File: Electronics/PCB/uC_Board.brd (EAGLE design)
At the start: 100 x 80 mm, 12 parts

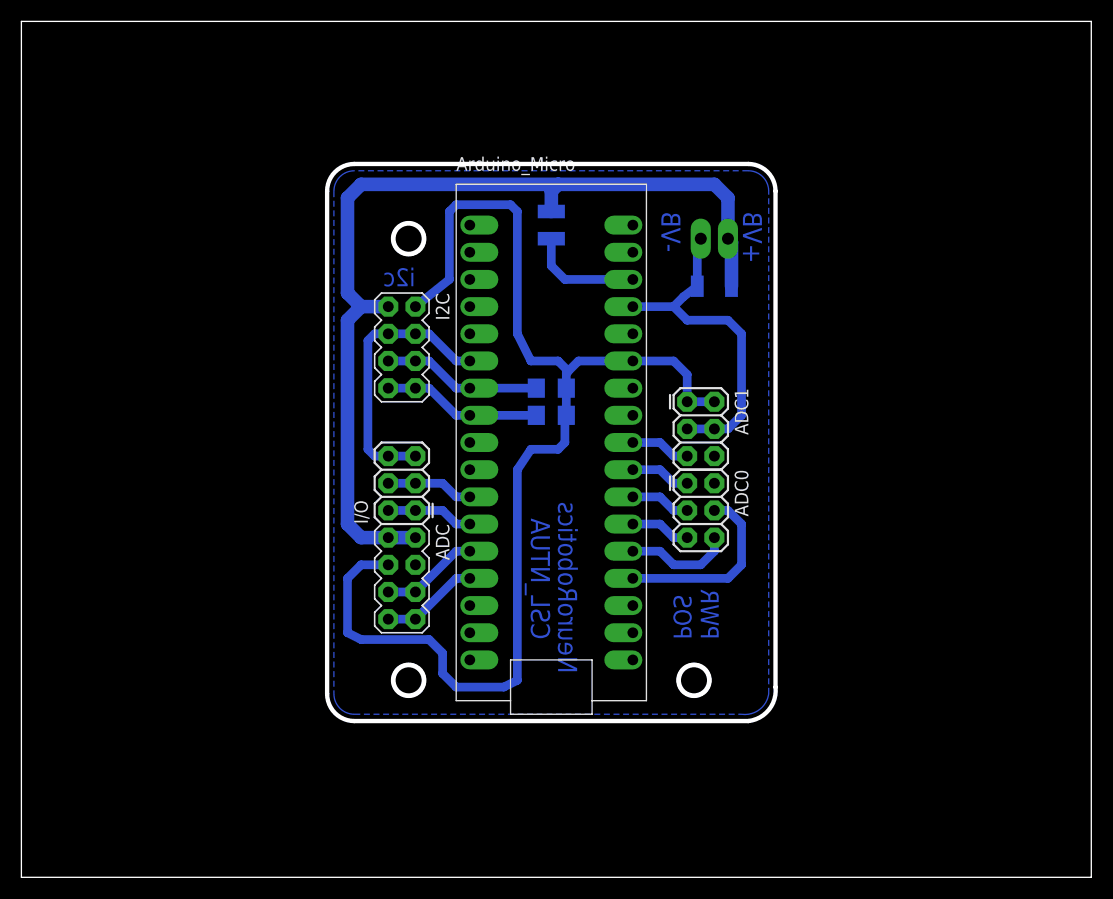
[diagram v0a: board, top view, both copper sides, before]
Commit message: Add new PCB for RC and AX12 servo.
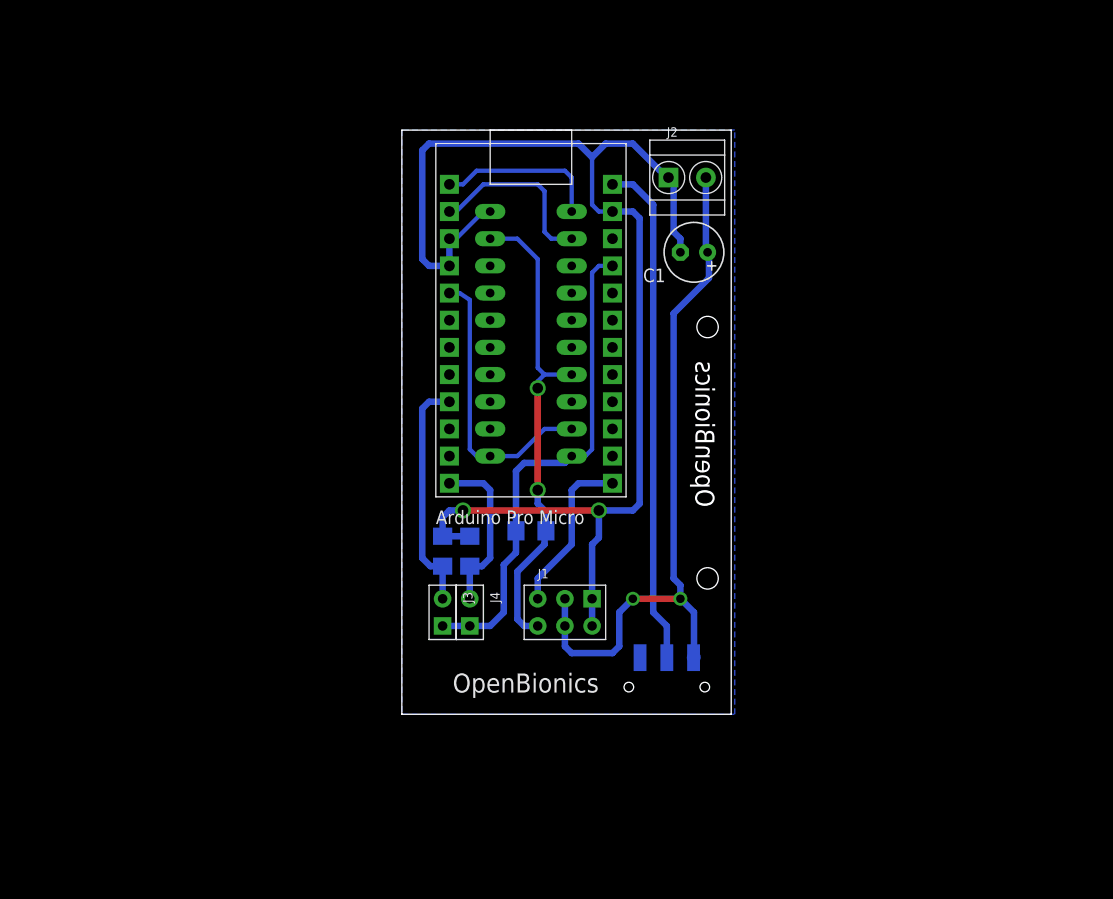
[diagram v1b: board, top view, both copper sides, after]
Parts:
- removed ADC, I2C: M04X2, SparkFun-Connectors:2X4
- removed ADC0, I/O: 0, SparkFun-Connectors:2X3
- removed ADC1: 1, SparkFun-Connectors:2X3
- removed FRAME1: FRAME-LETTER, SparkFun-Aesthetics:CREATIVE_COMMONS
- removed POWER: power, SparkFun-Connectors:1X02_LONGPADS
- removed PWR_JMP: pwr_jmp, jumper:SJW
- removed U$1: uC, Arduino_Micro:ARDUINO_MICRO
- added ARDUINO_MICRO: ARDUINO_PRO_MICROARDUINO_BOARD, OpenBionics:ARDUINO_MICRO_PRO
- added IC1: 74LS241N, 74xx-eu:DIL20
- added J1: 1, Connector:2X3P-2.54-65/35MIL
- added J2: SCREW-TERMINAL-2P-3470070P1, Connector:2P-3.5
- added J3: 2, Connector:2P-2.54-65/35MIL
- added J4: 3, Connector:2P-2.54-65/35MIL
- added R3: 10k, SparkFun-Passives:1206
- added S1: 1, SparkFun-Electromechanical:SWITCH-SPDT-SMD
- C1: value 4.7u -> 100u; device SparkFun-Capacitors:1210 -> rcl:E2,5-6
- moved R2 16.3 mm to (39.4, 30.5), turned to 270 degrees
- moved R1 13.5 mm to (47.6, 32.4)
- moved C1 3.70 mm to (62.9, 58.4), flipped to the top, turned to 180 degrees
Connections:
- removed net 5V: ADC.3, ADC1.1, ADC1.2, I2C.2, R1.1, R2.1, U$1.29
- removed net ADC0: ADC0.4, U$1.21
- removed net ADC1: ADC0.6, U$1.22
- removed net ADC2: ADC0.5, U$1.23
- removed net ADC3: ADC0.3, U$1.24
- removed net ADC4: ADC0.1, U$1.25
- removed net ADC5: ADC1.5, U$1.26
- removed net ADC6: ADC.5, ADC.6, U$1.13
- removed net ADC7: ADC.7, ADC.8, U$1.14
- removed net I/O_0: I/O.1, I/O.2, U$1.12
- removed net PULSE: I/O.3, I/O.4, U$1.11
- removed net SCL: I2C.7, I2C.8, R2.2, U$1.8
- removed net SDA: I2C.5, I2C.6, R1.2, U$1.7
- removed net VBAT+: ADC.1, ADC.2, C1.1, I2C.1, POWER.2, PWR_JMP.1
- removed net V_IN: PWR_JMP.2, U$1.32
- new net BUTTON1: ARDUINO_MICRO.9, J3.2, R2.2
- new net BUTTON2: ARDUINO_MICRO.12, J4.2, R3.2
- new net C_DATA: ARDUINO_MICRO.5, IC1.1, IC1.19
- new net DATA: IC1.17, IC1.9, J1.4, R1.1
- new net IO1: ARDUINO_MICRO.13, J1.3
- new net N$1: ARDUINO_MICRO.24, S1.2
- new net RX: ARDUINO_MICRO.2, IC1.12
- new net TX: ARDUINO_MICRO.1, IC1.11
- new net VCC: ARDUINO_MICRO.21, IC1.20, J3.1, J4.1, R1.2
- new net VS: C1.+, J1.2, J1.5, J2.2, S1.3
- net GND: now also ARDUINO_MICRO.23, ARDUINO_MICRO.3, ARDUINO_MICRO.4, C1.-, IC1.10, J1.1, J1.6, J2.1, R2.1, R3.1; no longer ADC1.3, ADC1.4, C1.2, I/O.5, I/O.6, I2C.3, I2C.4, POWER.1, U$1.31, U$1.6
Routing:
- net 5V: track 113.7 -> 0.00 mm
- net VBAT+: track 88.8 -> 0.00 mm
- net VS: track 0.00 -> 66.7 mm, vias 0 -> 2
- net GND: track 57.7 -> 123.7 mm, vias 0 -> 2
- net N$1: track 0.00 -> 47.5 mm
- net VCC: track 0.00 -> 46.6 mm
- net DATA: track 0.00 -> 45.5 mm, vias 0 -> 2
- net C_DATA: track 0.00 -> 26.9 mm
- net BUTTON1: track 0.00 -> 22.0 mm
- net ADC0: track 17.6 -> 0.00 mm
- net RX: track 0.00 -> 16.8 mm
- net BUTTON2: track 0.00 -> 15.7 mm
- net IO1: track 0.00 -> 15.5 mm
- net TX: track 0.00 -> 15.4 mm
- net SDA: track 14.9 -> 0.00 mm
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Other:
- board size 100 x 80 mm -> 30.8 x 54.6 mm
- board text added: "OpenBionics"
- board text removed: "+VB"
- board text removed: "-VB"
- board text removed: "CSL_NTUA"
- board text removed: "NeuroRobotics"
- board text removed: "POS"
- board text removed: "PWR"
- board text removed: "i2c"

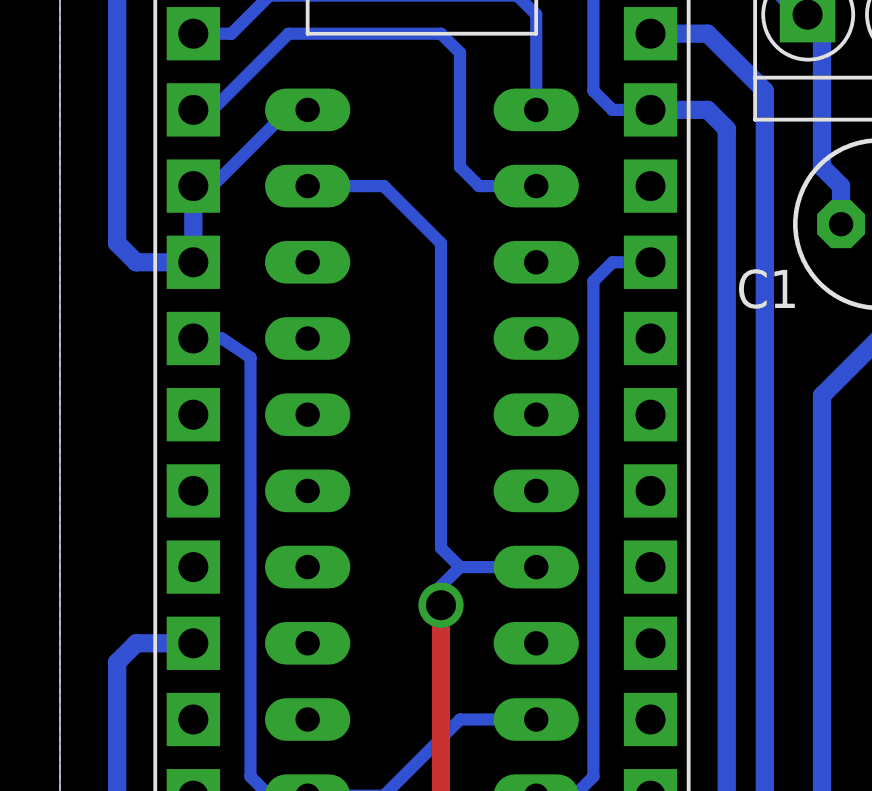
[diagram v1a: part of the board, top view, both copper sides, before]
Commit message: Repair the PCB,wrong connection with Rx in AX12 servo.
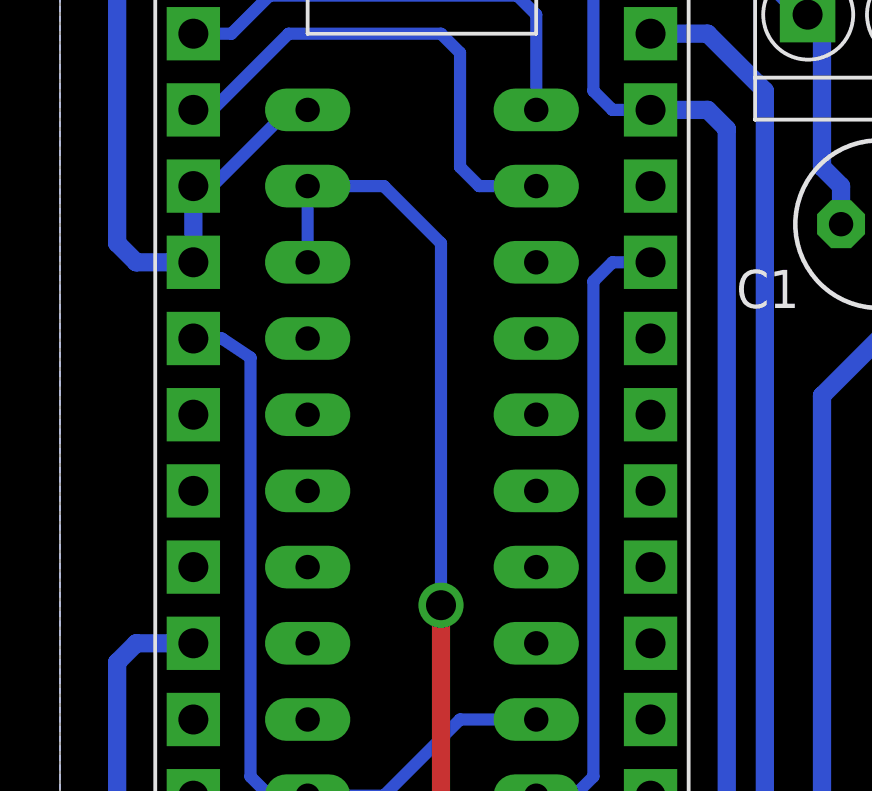
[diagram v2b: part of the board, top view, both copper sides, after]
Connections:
- net DATA: now also IC1.8; no longer IC1.17
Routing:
- net DATA: track 45.5 -> 45.0 mm
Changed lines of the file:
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@@
 <layer number="17" name="Pads" color="2" fill="1" visible="yes" active="yes"/>
 <layer number="18" name="Vias" color="2" fill="1" visible="yes" active="yes"/>
-<layer number="19" name="Unrouted" color="6" fill="1" visible="no" active="yes"/>
+<layer number="19" name="Unrouted" color="6" fill="1" visible="yes" active="yes"/>
 <layer number="20" name="Dimension" color="15" fill="1" visible="yes" active="yes"/>
 <layer number="21" name="tPlace" color="7" fill="1" visible="yes" active="yes"/>
 <layer number="22" name="bPlace" color="7" fill="1" visible="yes" active="yes"/>
-<layer number="23" name="tOrigins" color="15" fill="1" visible="no" active="yes"/>
-<layer number="24" name="bOrigins" color="15" fill="1" visible="no" active="yes"/>
+<layer number="23" name="tOrigins" color="15" fill="1" visible="yes" active="yes"/>
+<layer number="24" name="bOrigins" color="15" fill="1" visible="yes" active="yes"/>
 <layer number="25" name="tNames" color="7" fill="1" visible="yes" active="yes"/>
 <layer number="26" name="bNames" color="7" fill="1" visible="yes" active="yes"/>
@@
 <contactref element="R1" pad="1"/>
 <contactref element="IC1" pad="9"/>
-<contactref element="IC1" pad="17"/>
 <via x="48.26" y="45.72" extent="1-16" drill="1" diameter="1.27" shape="square"/>
 <wire x1="48.26" y1="45.72" x2="48.26" y2="36.195" width="0.6096" layer="1"/>
@@
 <wire x1="46.355" y1="24.13" x2="46.99" y2="23.495" width="0.6096" layer="16"/>
 <wire x1="46.99" y1="23.495" x2="48.26" y2="23.495" width="0.6096" layer="16"/>
-<wire x1="48.26" y1="45.72" x2="48.26" y2="46.355" width="0.4064" layer="16"/>
-<wire x1="48.26" y1="46.355" x2="48.895" y2="46.99" width="0.4064" layer="16"/>
-<wire x1="48.895" y1="46.99" x2="51.435" y2="46.99" width="0.4064" layer="16"/>
-<wire x1="48.895" y1="46.99" x2="48.26" y2="47.625" width="0.4064" layer="16"/>
 <wire x1="43.815" y1="59.69" x2="46.355" y2="59.69" width="0.4064" layer="16"/>
 <wire x1="46.355" y1="59.69" x2="48.26" y2="57.785" width="0.4064" layer="16"/>
-<wire x1="48.26" y1="57.785" x2="48.26" y2="47.625" width="0.4064" layer="16"/>
+<wire x1="48.26" y1="57.785" x2="48.26" y2="45.72" width="0.4064" layer="16"/>
+<contactref element="IC1" pad="8"/>
+<wire x1="43.815" y1="59.69" x2="43.815" y2="57.15" width="0.4064" layer="16"/>
 </signal>
 <signal name="TX">
